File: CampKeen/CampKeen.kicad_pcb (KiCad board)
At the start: 4 copper layers, 177.8 x 142.2 mm, 194 parts, among them IC1 LM2597MX-ADJ_NOPB, IC2 LM2670SX-5.0_NOPB, IC3 DS3231SN#, IC4 TL071CP, J1 Vin, J2 CAC, J3 VAC, J4 Screw_Terminal_01x04, J5 GenEnclosure, J6 GenHeadL, J7 GenHeadR, K1 DIP05-1A72-12L, K2 DIP05-1A72-12L, K3 DIP05-1A72-12L, K4 DIP05-1A72-12L, P1 Power, P10 CONN_01X01, P11 CONN_01X01, P12 CONN_01X01, P13 CONN_01X01, P2 Analog, P3 Analog, P4 Digital, P5 PWM, P6 PWM, P7 Communication, P8 CONN_01X01, P9 CONN_01X01, Q1 BC547, Q10 2N7000, Q11 2N7000, Q12 2N7000, Q13 2N7000, Q14 2N7000, Q15 IRF510, Q16 2N7000, Q17 IRF510, Q18 2N7000, Q19 IRF510, Q2 2N7000, Q20 2N7000, Q21 IRF510, Q22 BC547, Q23 2N7000, Q24 IRF510, Q25 2N7000, Q26 2N7000, Q27 IRF510, Q28 2N7000, Q29 IRF510, Q3 2N7000, Q30 2N7000, Q31 IRF510, Q32 BC547, Q33 2N7000, Q34 IRF510, Q35 2N7000, Q36 IRF510, Q37 2N7000, Q38 IRF510, Q39 IRF510, Q4 2N7000, Q40 IRF9Z34NPBF, Q5 2N7000, Q6 BC547, Q7 2N7000, Q8 2N7000, Q9 2N7000, T1 F24-045-C2, U2 MAX232

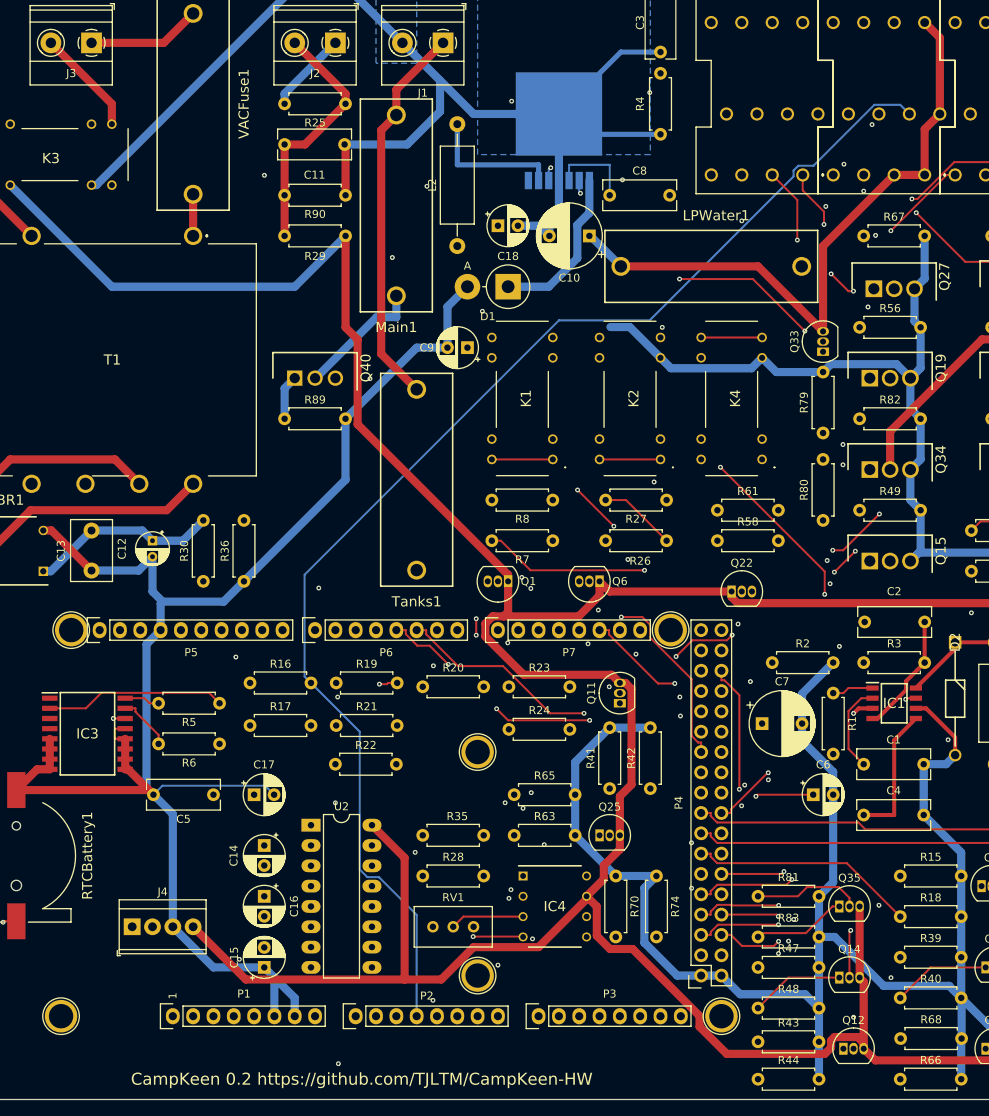
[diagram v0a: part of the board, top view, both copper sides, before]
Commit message: 0.2.1 fixed a left over trace. 0.2 will need a jumper wire to make sure a gnd trace won't burn out.
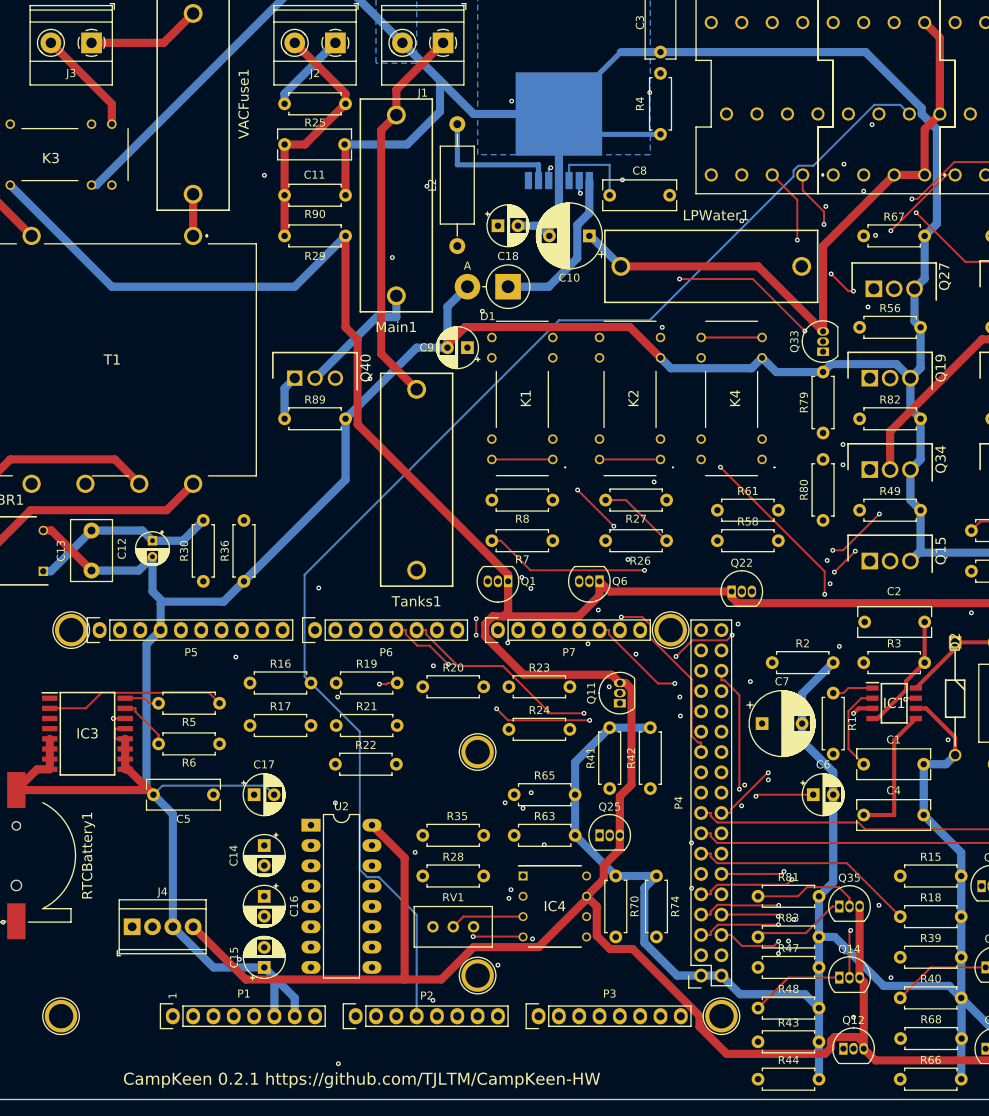
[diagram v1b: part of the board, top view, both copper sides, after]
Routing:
- net GND: track 1250.1 -> 1324.7 mm
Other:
- board text added: "CampKeen 0.2.1 https://github.com/TJLTM/CampKeen-HW"
- board text removed: "CampKeen 0.2 https://github.com/TJLTM/CampKeen-HW"

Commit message: 0.3 wip plans for making more use of space and possibly moving some stuff around
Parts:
- removed Q34: IRF510, SamacSys_Parts:TO254P465X1024X2050-3P
- removed R82: 1M, Resistor_THT:R_Axial_DIN0207_L6.3mm_D2.5mm_P7.62mm_Horizontal
- R1, R10, R11, R12, R13, R14, R15, R16, R17, R18, R19, R2, R20, R21, R22, R23, R24, R25, R26, R27, R28, R29, R3, R30, R31, R32, R33, R34, R35, R36, R37, R38, R39, R4, R40, R41, R42, R43, R44, R45, R46, R47, R48, R49, R5, R50, R51, R52, R53, R54, R55, R56, R57, R58, R59, R6, R60, R61, R62, R63, R64, R65, R66, R67, R68, R69, R7, R70, R71, R72, R73, R74, R75, R76, R77, R78, R79, R8, R80, R81, R83, R84, R85, R86, R87, R88, R89, R9, R90: footprint Resistor_THT:R_Axial_DIN0207_L6.3mm_D2.5mm_P7.62mm_Horizontal -> Resistor_THT:R_Axial_DIN0207_L6.3mm_D2.5mm_P2.54mm_Vertical
- moved C1 249.8 mm to (-80.8, 50.8)
- moved C2 249.8 mm to (-73.2, 33.0)
- moved C4 249.8 mm to (-80.8, 57.1)
- moved C7 249.8 mm to (-93.5, 45.7)
- moved D2 249.8 mm to (-69.3, 35.6)
- moved IC1 249.8 mm to (-77.0, 43.2)
- moved L1 249.8 mm to (-64.3, 35.6)
- moved R2 249.8 mm to (-92.2, 38.1)
- moved R3 249.8 mm to (-80.8, 38.1)
- moved C6 249.8 mm to (-87.1, 54.6)
- moved R1 249.8 mm to (-84.6, 41.9)
- moved Tanks1 124.8 mm to (151.6, -35.6)
- moved LPWater1 91.8 mm to (164.3, -35.6), turned to 90 degrees
- moved Main1 89.2 mm to (138.9, -35.6)
- moved R44 76.2 mm to (221.5, 137.7), turned to 90 degrees
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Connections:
- IO1 pad 7: Net-(IO1-Pad7) -> +9V
- Q31 pad 2: Net-(IO1-Pad7) -> Net-(O1-Pad10)
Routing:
- net GND: track 1324.7 -> 0.00 mm, vias 6 -> 0
- net +5V: track 782.5 -> 0.00 mm
- net Net-(Q8-Pad2): track 231.4 -> 0.00 mm, vias 3 -> 0
- net +12V: track 227.6 -> 0.00 mm, vias 3 -> 0
- net Net-(IO1-Pad3): track 226.0 -> 0.00 mm, vias 1 -> 0
- net Net-(IO1-Pad4): track 201.3 -> 0.00 mm, vias 2 -> 0
- net Net-(I1-Pad2): track 195.4 -> 0.00 mm, vias 5 -> 0
- net /A1: track 193.5 -> 0.00 mm, vias 2 -> 0
- net /A4: track 185.4 -> 0.00 mm, vias 2 -> 0
- net Net-(Q9-Pad2): track 182.0 -> 0.00 mm, vias 4 -> 0
- net /A9: track 181.6 -> 0.00 mm, vias 1 -> 0
- net Net-(I1-Pad12): track 180.8 -> 0.00 mm, vias 1 -> 0
- net /A2: track 178.4 -> 0.00 mm
- net Net-(IO1-Pad1): track 178.3 -> 0.00 mm, vias 2 -> 0
- net Net-(I1-Pad9): track 168.5 -> 0.00 mm, vias 2 -> 0
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- removed copper zone on B.Cu, net GND
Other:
- board text added: "CampKeen 0.3 https://github.com/TJLTM/CampKeen-HW"
- board text removed: "CampKeen 0.2.1 https://github.com/TJLTM/CampKeen-HW"

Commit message: tewst
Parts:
- moved C1 20.3 mm to (-60.5, 50.8)
- moved R3 20.3 mm to (-60.5, 38.1)
- moved C2 20.3 mm to (-52.8, 33.0)
- moved D2 20.3 mm to (-49.0, 35.6)
- moved IC1 20.3 mm to (-56.6, 43.2)
- moved L1 20.3 mm to (-43.9, 35.6)

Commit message: working on the PCB for 0.3
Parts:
- removed RV1: 500K, Potentiometer_THT:Potentiometer_Bourns_3296W_Vertical
- added IC5: LM2904N_NOPB, SamacSys_Parts:DIP794W53P254L959H508Q8N, F.Cu at (91.9, 67.3)
- added R82: 40K, Resistor_THT:R_Axial_DIN0207_L6.3mm_D2.5mm_P2.54mm_Vertical, F.Cu at (89.4, 77.5)
- added U1: TL431LP, Package_TO_SOT_THT:TO-92_Inline, F.Cu at (84.3, 40.6)
- IC4: value TL071CP -> INA849DR; footprint SamacSys_Parts:DIP794W53P254L959H508Q8N -> SamacSys_Parts:SOIC127P600X175-8N
- R25: footprint Resistor_THT:R_Axial_DIN0207_L6.3mm_D2.5mm_P2.54mm_Vertical -> Resistor_THT:R_Axial_DIN0207_L6.3mm_D2.5mm_P10.16mm_Horizontal
- R29: value 100k -> 1K
- moved Tanks1 129.7 mm to (192.3, 87.6), turned to 180 degrees
- moved LPWater1 120.2 mm to (150.4, 83.8), turned to 270 degrees
- moved R10 113.7 mm to (164.3, 128.8)
- moved R9 113.7 mm to (159.3, 128.8)
- moved Q2 113.3 mm to (160.5, 123.2)
- moved R11 113.3 mm to (159.3, 117.3)
- moved R12 113.3 mm to (164.3, 117.3)
- moved Q3 113.1 mm to (160.5, 111.8)
- moved C4 101.3 mm to (19.6, 71.1)
- moved C6 101.3 mm to (13.2, 68.6)
- moved C7 101.3 mm to (6.86, 59.7)
- moved R1 101.3 mm to (15.7, 55.9)
- moved R2 101.3 mm to (8.13, 52.1)
- moved IC4 89.4 mm to (94.5, 48.3), turned to 270 degrees
- moved IC1 81.0 mm to (23.4, 55.9)
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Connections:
- C11 pad 1: /A12 -> Net-(C11-Pad1)
- C11 pad 2: GND -> Net-(C11-Pad2)
- IC4 pad 1: (no net) -> Net-(C11-Pad1)
- IC4 pad 2: /A0 -> (no net)
- IC4 pad 3: Net-(IC4-Pad3) -> (no net)
- IC4 pad 4: GND -> Net-(C11-Pad2)
- IC4 pad 5: (no net) -> GND
- IC4 pad 6: /A0 -> Net-(IC4-Pad6)
- IC4 pad 7: +5V -> /A12
- IC4 pad 8: (no net) -> +5V
- J2 pad 1: Net-(J2-Pad1) -> Net-(C11-Pad1)
- J2 pad 2: /A12 -> Net-(C11-Pad2)
- R25 pad 1: /A12 -> Net-(C11-Pad2)
- R25 pad 2: Net-(J2-Pad1) -> Net-(C11-Pad1)
- R29 pad 1: /A12 -> Net-(IC5-Pad3)
- R90 pad 2: /A12 -> Net-(IC4-Pad6)
- T1 pad 5: Net-(BR1-Pad4) -> Net-(BR1-Pad3)
- T1 pad 6: Net-(BR1-Pad3) -> Net-(BR1-Pad4)
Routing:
- net +5V: track 0.00 -> 391.7 mm
- net GND: track 0.00 -> 120.3 mm
- net Net-(O1-Pad1): track 0.00 -> 92.6 mm
- net Net-(O1-Pad3): track 0.00 -> 75.4 mm
- net Net-(O1-Pad8): track 0.00 -> 64.8 mm
- net Net-(O1-Pad9): track 0.00 -> 62.2 mm
- net Net-(O1-Pad6): track 0.00 -> 61.1 mm
- net +12V: track 0.00 -> 59.3 mm
- net Net-(O1-Pad2): track 0.00 -> 49.1 mm
- net Net-(O1-Pad7): track 0.00 -> 45.7 mm
- net Net-(O1-Pad5): track 0.00 -> 36.5 mm
- net Net-(O1-Pad12): track 0.00 -> 35.3 mm
- net Net-(O1-Pad4): track 0.00 -> 30.9 mm
- net Net-(O1-Pad10): track 0.00 -> 19.2 mm
- net Net-(K3-Pad1): track 0.00 -> 18.2 mm
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- added copper zone on B.Cu, net (none)
- added copper zone on B.Cu, net GND
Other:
- board text added: "CampKeen https://github.com/TJLTM/CampKeen-HW"
- board text added: "Holding Tank Sensors"
- board text added: "LPG"
- board text added: "NTC TEMP"
- board text added: "OUTPUTS"
- board text added: "Version: 0.3"
- board text added: "Water"
- board text removed: "CampKeen 0.3 https://github.com/TJLTM/CampKeen-HW"

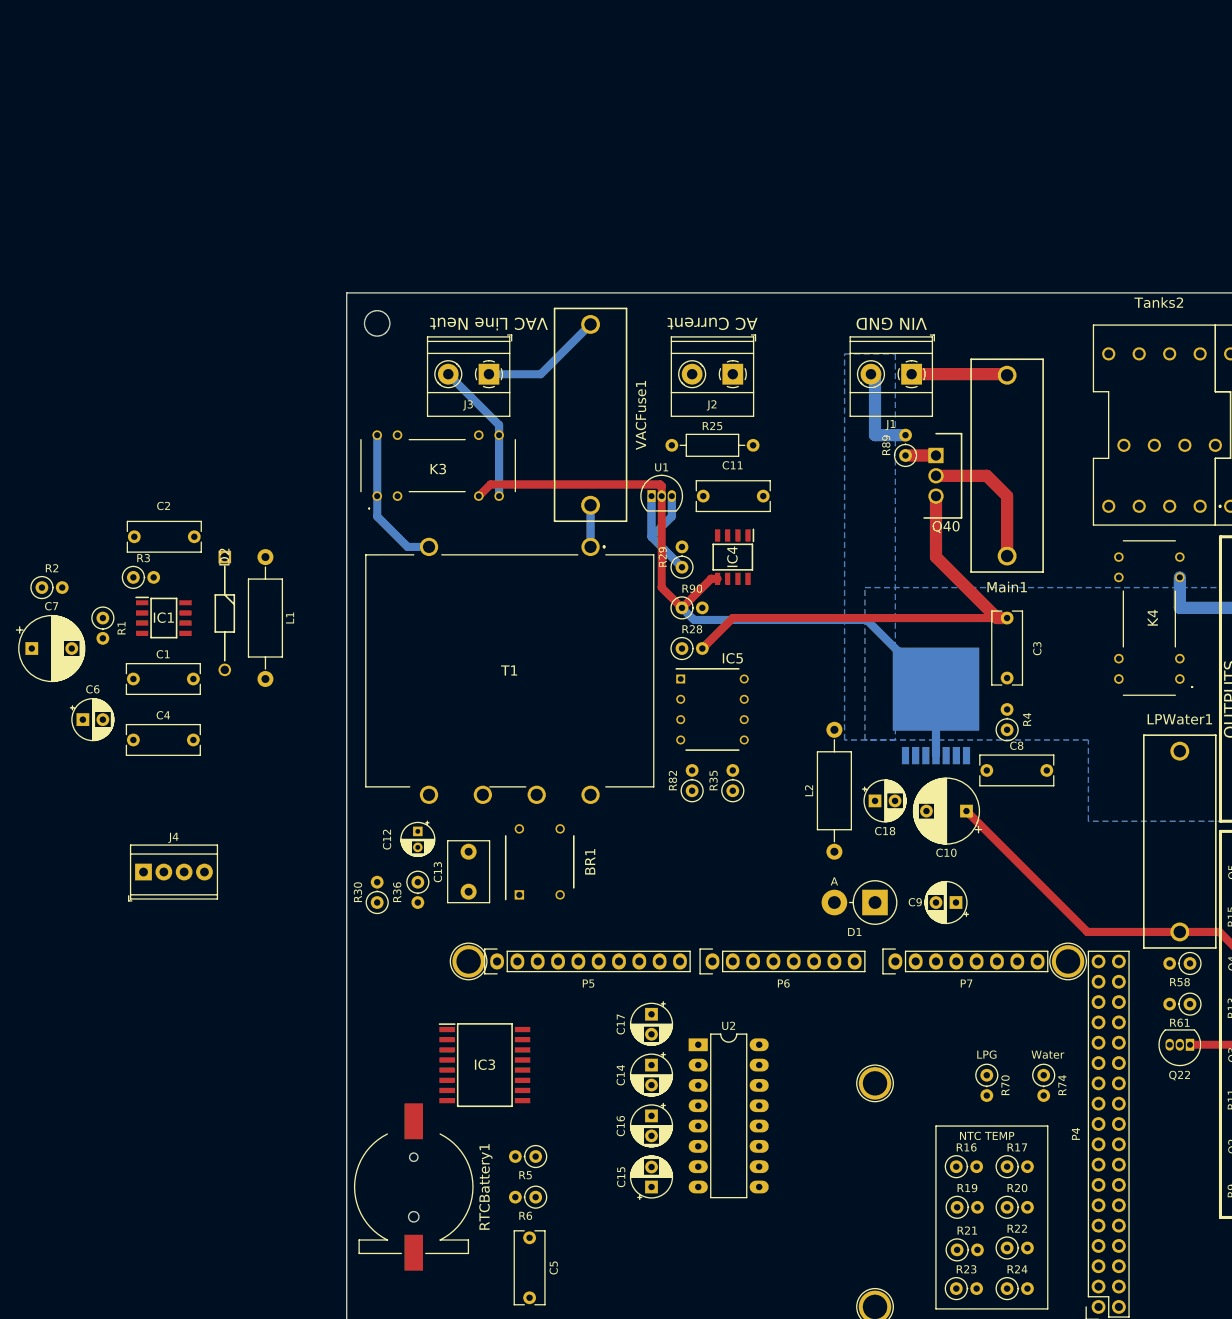
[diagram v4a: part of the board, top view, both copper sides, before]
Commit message: 0.3 fixing a bug found in 0.2 hardware.
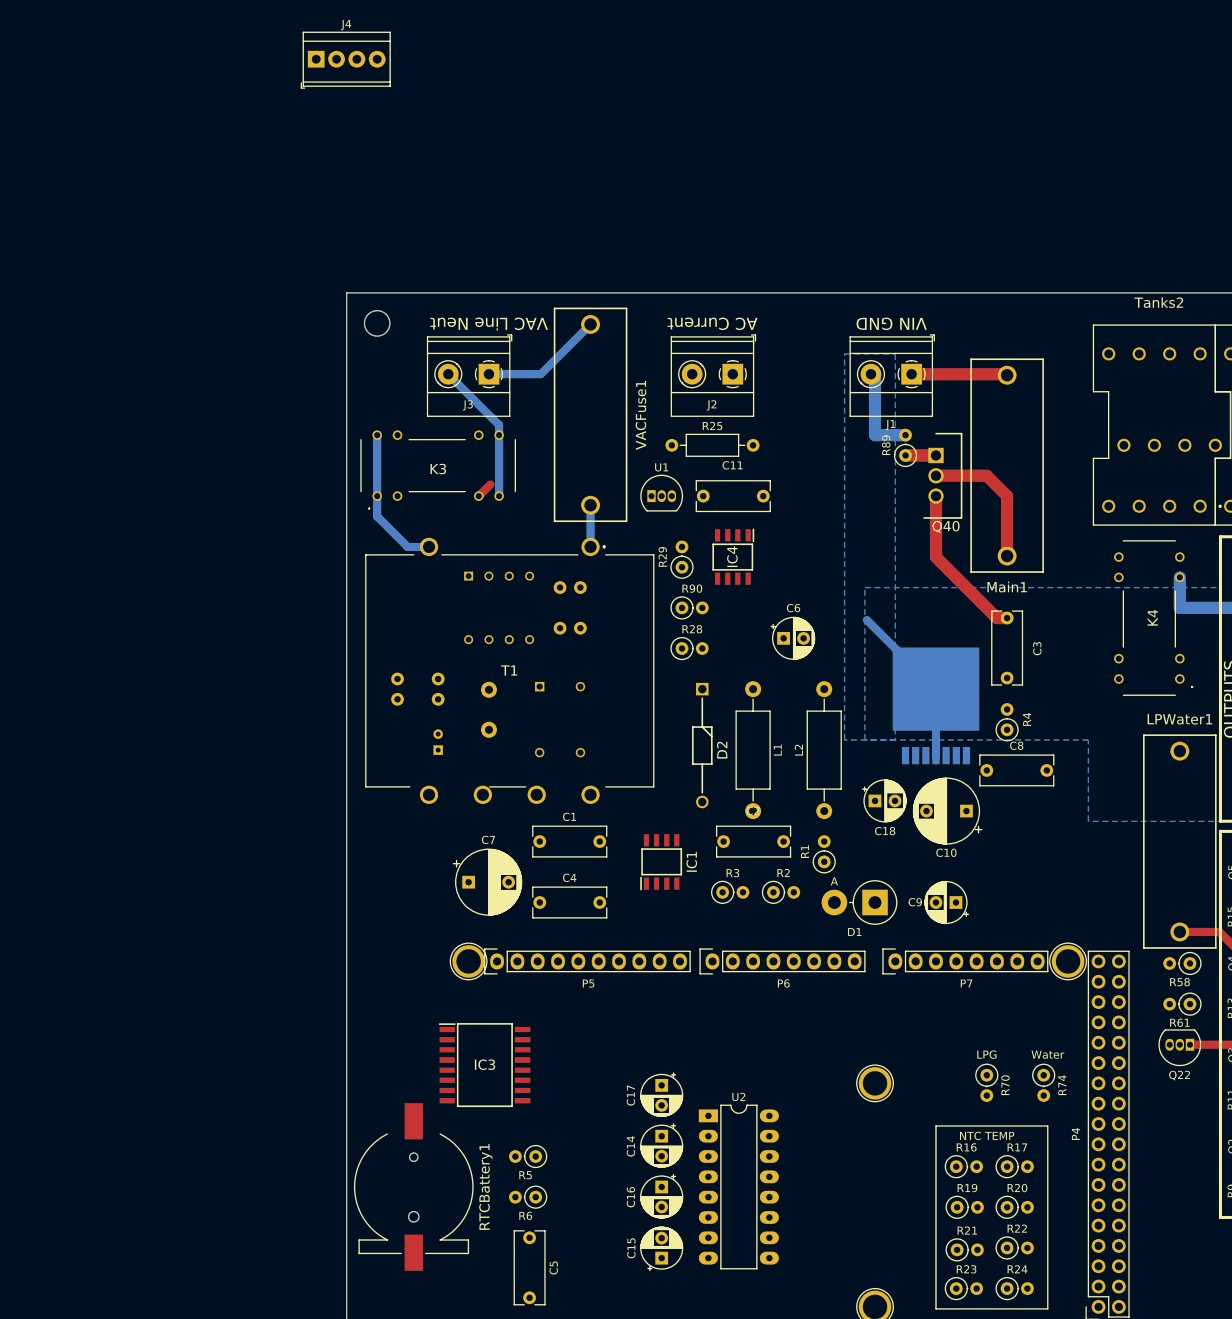
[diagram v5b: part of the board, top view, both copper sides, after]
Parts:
- BR1, C12, C13, IC5, R30, R35, R36: moved to B.Cu
- R82: value 40K -> 20K; moved to B.Cu
- moved J4 103.9 mm to (42.4, -14.0)
- moved R2 99.1 mm to (99.6, 90.2)
- moved R1 95.2 mm to (105.9, 86.4), turned to 90 degrees
- moved C6 88.2 mm to (100.8, 58.4)
- moved R3 83.5 mm to (93.2, 90.2)
- moved C2 82.9 mm to (100.8, 83.8)
- moved IC1 69.3 mm to (85.6, 86.4), turned to 90 degrees
- moved L1 63.2 mm to (97.0, 64.8)
- moved C7 61.9 mm to (61.5, 88.9)
- moved D2 61.9 mm to (90.7, 64.8)
- moved C1 54.7 mm to (70.4, 83.8)
- moved C4 54.7 mm to (70.4, 91.4)
- moved IC5 29.5 mm to (65.3, 54.6), turned to 270 degrees
- moved R82 29.0 mm to (75.4, 52.1), turned to 180 degrees
- moved R30 28.1 mm to (52.6, 63.5), turned to 270 degrees
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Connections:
- K1 pad 2: Net-(K1-Pad2) -> +5V
- K1 pad 6: GND -> Net-(K1-Pad6)
- K2 pad 2: Net-(K2-Pad2) -> +5V
- K2 pad 6: GND -> Net-(K2-Pad6)
- Q1 pad 1: +5V -> Net-(K1-Pad6)
- Q1 pad 3: Net-(K1-Pad2) -> GND
- Q32 pad 1: +5V -> Net-(O1-Pad11)
- Q32 pad 3: Net-(O1-Pad11) -> GND
- Q6 pad 1: +5V -> Net-(K2-Pad6)
- Q6 pad 3: Net-(K2-Pad2) -> GND
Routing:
- net GND: track 120.3 -> 52.9 mm
- net +12V: track 59.3 -> 19.7 mm
- net +5V: track 391.7 -> 358.8 mm
- net Net-(IC5-Pad3): track 16.6 -> 0.00 mm
